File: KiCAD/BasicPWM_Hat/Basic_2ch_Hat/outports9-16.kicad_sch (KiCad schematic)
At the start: 36 parts, among them IC2 SN74HC244N, J10 G D V, J11 G D V, J12 G D V, J13 G D V, J14 G D V, J15 G D V, J16 G D V, J9 G D V

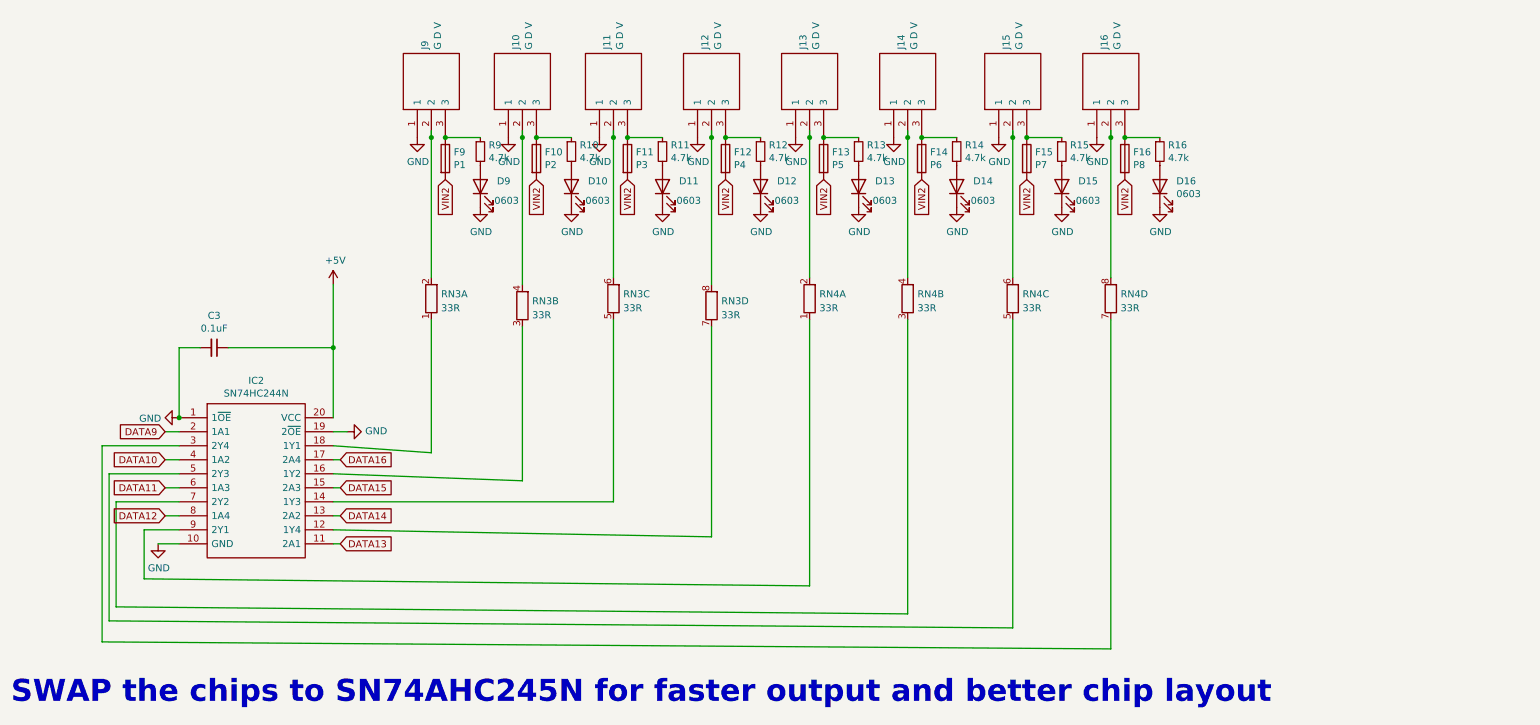
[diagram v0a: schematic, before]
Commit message: swap chips to better speed / layout
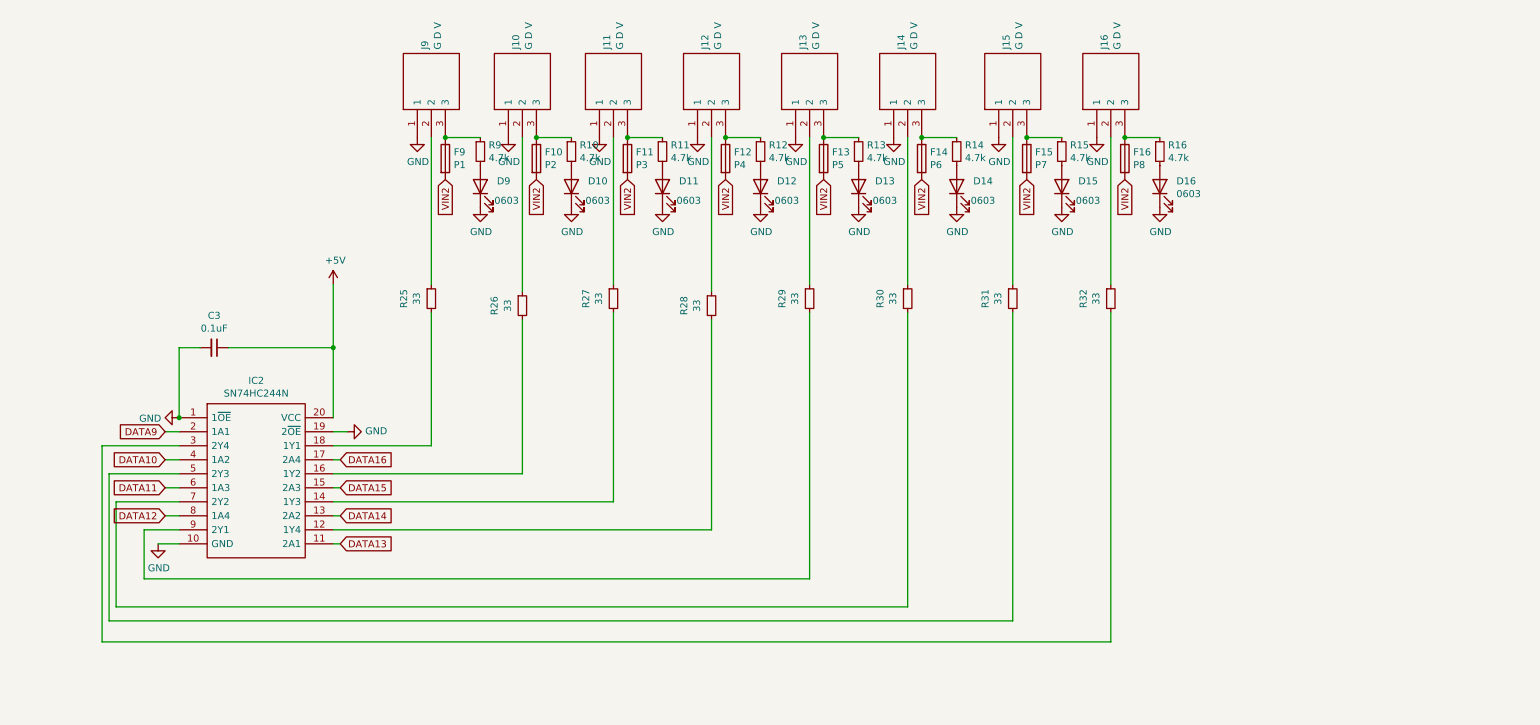
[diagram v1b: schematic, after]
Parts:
- removed RN3, RN4: 33R, Resistor_THT:R_Array_SIP8, symbol Device:R_Pack04_SIP_Split
- added R25, R26, R27, R28, R29, R30, R31, R32: 33, Resistor_SMD:R_0805_2012Metric, symbol Device:R_Small
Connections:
- net at J9.2: now also R25.1
- net at IC2.12 (1Y4): now also R28.2
- net at IC2.14 (1Y3): now also R27.2
- net at IC2.16 (1Y2): now also R26.2
- net at IC2.18 (1Y1): now also R25.2
- net at IC2.3 (2Y4): now also R32.2
- net at IC2.5 (2Y3): now also R31.2
- net at IC2.7 (2Y2): now also R30.2
- net at IC2.9 (2Y1): now also R29.2
- net at J10.2: now also R26.1
- net at J11.2: now also R27.1
- net at J12.2: now also R28.1
- net at J13.2: now also R29.1
- net at J14.2: now also R30.1
- net at J15.2: now also R31.1
- net at J16.2: now also R32.1
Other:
- note removed: "SWAP the chips to SN74AHC245N for faster output and better chip layout"
